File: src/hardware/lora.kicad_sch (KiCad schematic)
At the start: 19 parts

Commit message: Selected GPIO
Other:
- note added: "tcxoVoltage: 0x02 (1.8V)"
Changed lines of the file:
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@@
+		)
+	)
+	(text "tcxoVoltage: 0x02 (1.8V)"
+		(exclude_from_sim no)
+		(at 74.422 86.36 0)
+		(effects
+			(font
+				(size 1.27 1.27)
+			)
 		)
 	)

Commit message: Selected GPIO
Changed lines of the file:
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@@
 		)
 		(property "Value" "GND"
-			(at 132.08 128.27 0)
-			(effects
-				(font
-					(size 1.27 1.27)
-				)
+			(at 134.62 124.4599 0)
+			(effects
+				(font
+					(size 1.27 1.27)
+				)
+				(justify left)
 			)
 		)
@@
 		)
 		(property "Value" "GND"
-			(at 107.95 97.79 0)
-			(effects
-				(font
-					(size 1.27 1.27)
-				)
+			(at 110.49 93.9799 0)
+			(effects
+				(font
+					(size 1.27 1.27)
+				)
+				(justify left)
 			)
 		)
@@
 		)
 		(property "Value" "GND"
-			(at 80.01 102.87 0)
-			(effects
-				(font
-					(size 1.27 1.27)
-				)
-			)
-		)
+			(at 82.55 99.0599 0)
+			(effects
+				(font
+					(size 1.27 1.27)
+				)
+				(justify left)
+			)
+		)

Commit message: LoRa Crystal Optional
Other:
- note added: "Optional"
- moved on the sheet: C?, Q?, R?, Y?

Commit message: Added Accelerometer Clock; Cleanup & Fixes
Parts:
- R?: value 100 -> 100Ω
- R?: value 220 -> 220Ω
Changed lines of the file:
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@@
 			)
 		)
-		(property "Value" "100"
+		(property "Value" "100Ω"
 			(at 67.31 128.2699 0)
 			(effects
@@
 		(fields_autoplaced yes)
 		(property "Reference" "R?"
-			(at 115.57 72.39 90)
-			(effects
-				(font
-					(size 1.27 1.27)
-				)
-			)
-		)
-		(property "Value" "220"
-			(at 115.57 74.93 90)
-			(effects
-				(font
+			(at 115.57 62.23 90)
+			(effects
+				(font
+					(size 1.27 1.27)
+				)
+			)
+		)
+		(property "Value" "220Ω"
+			(at 115.57 64.77 90)
+			(effects
+				(font

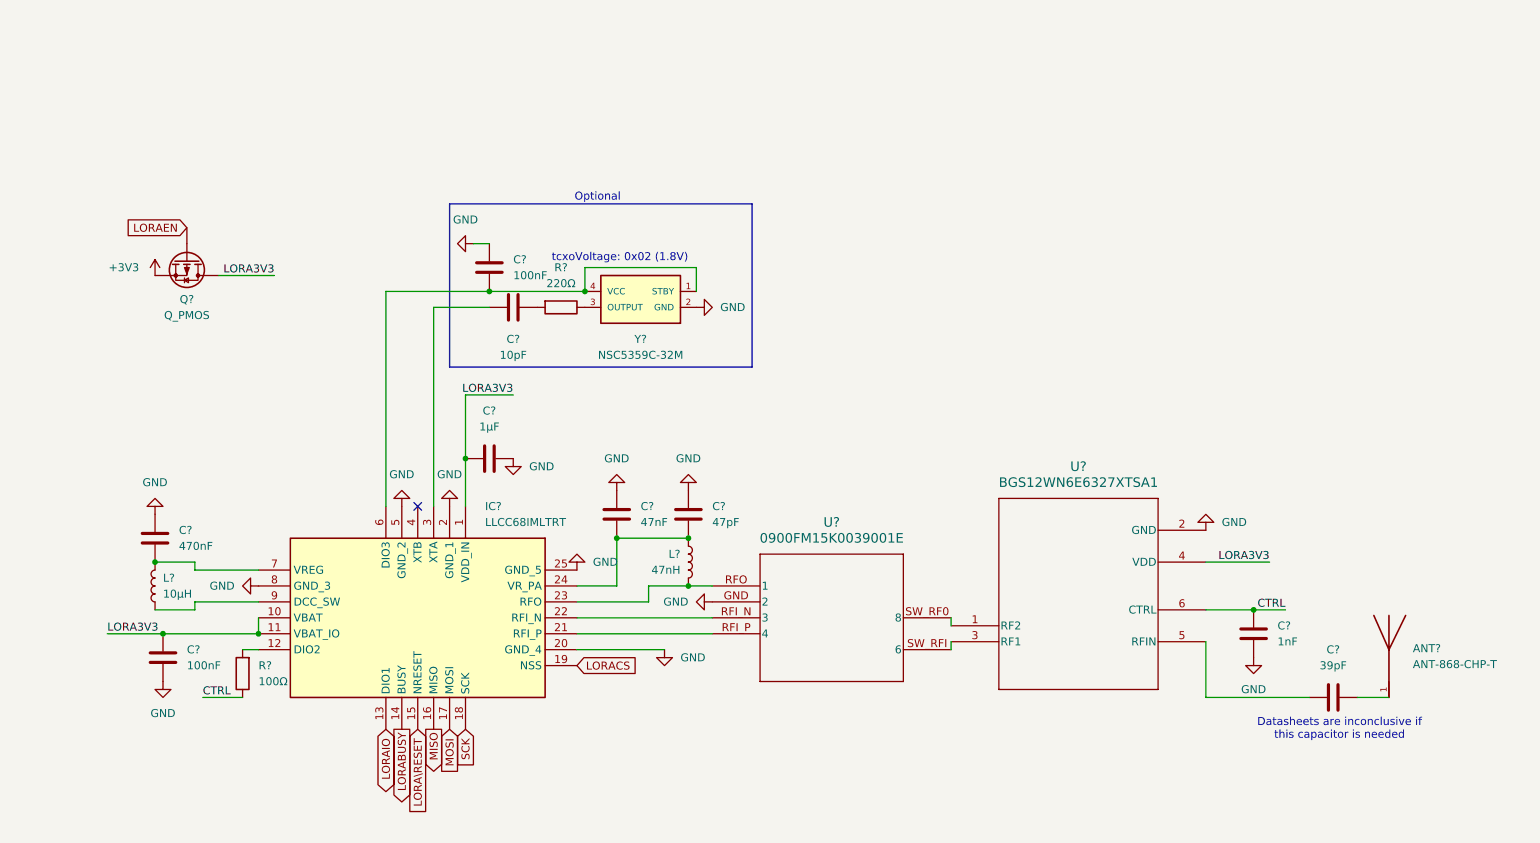
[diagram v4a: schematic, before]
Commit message: Cleanup & Fixes; Added footprints; Removed Light sensors
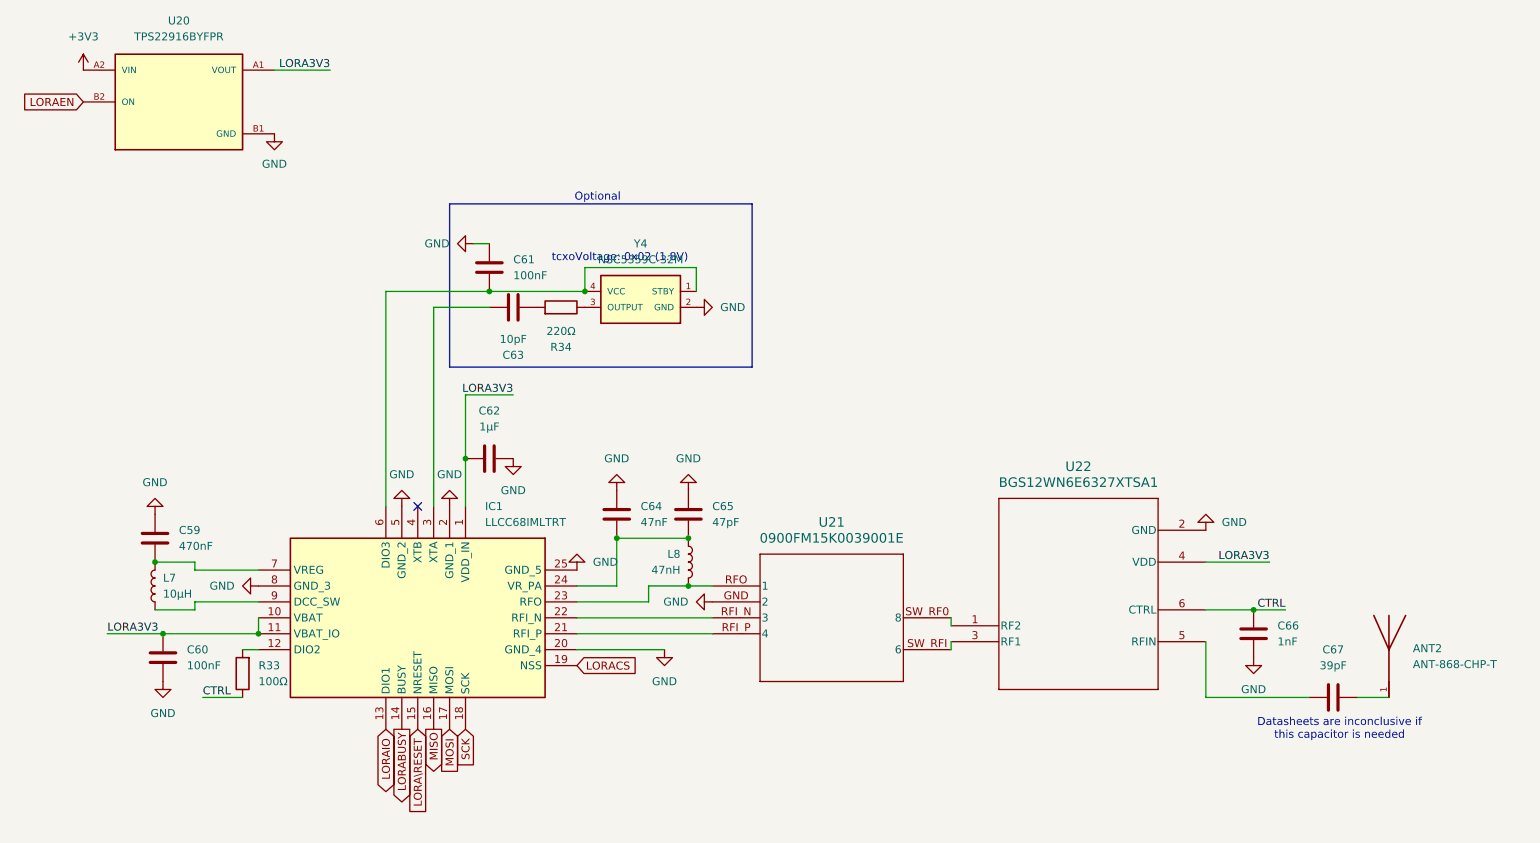
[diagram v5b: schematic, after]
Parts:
- removed Q?: Q_PMOS, symbol Device:Q_PMOS
- added U20: TPS22916BYFPR, Project:IC_TPS22916BYFPR, symbol TPS22916BYFPR:TPS22916BYFPR
- ANT2: renamed from ANT?; footprint ANT-868-CHP-T:XDCR_ANT-868-CHP-T -> Project:XTAL_ABS07-32.768KHZ-7-T
- C59, C60, C61, C62, C63, C64, C65, C66, C67: renamed from C?; footprint (none) -> Capacitor_SMD:C_0603_1608Metric
- IC1: renamed from IC?; footprint QFN50P400X400X100-25L-D -> Project:QFN50P400X400X100-25L-D
- L7, L8: renamed from L?; footprint (none) -> Inductor_SMD:L_0402_1005Metric
- R33, R34: renamed from R?; footprint (none) -> Resistor_SMD:R_0603_1608Metric
- U21: renamed from U?; footprint QFP20P0X0X31-0_JOT -> Project:QFP20P0X0X31-0_JOT
- U22: renamed from U?; footprint PG-TSNP-6-10_INF -> Project:PG-TSNP-6-10_INF
- Y4: renamed from Y?; footprint NSC5359C:NSC5359C -> Project:NSC5359C
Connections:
- net +3V3: now also U20.A2 (VIN)
- net GND: now also U20.B1 (GND)
- net LORA3V3: now also U20.A1 (VOUT)
- net LORAEN: now also U20.B2 (ON)

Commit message: Cleanup & Fixes; Changed GPIO; Added Camera; Added Microphone
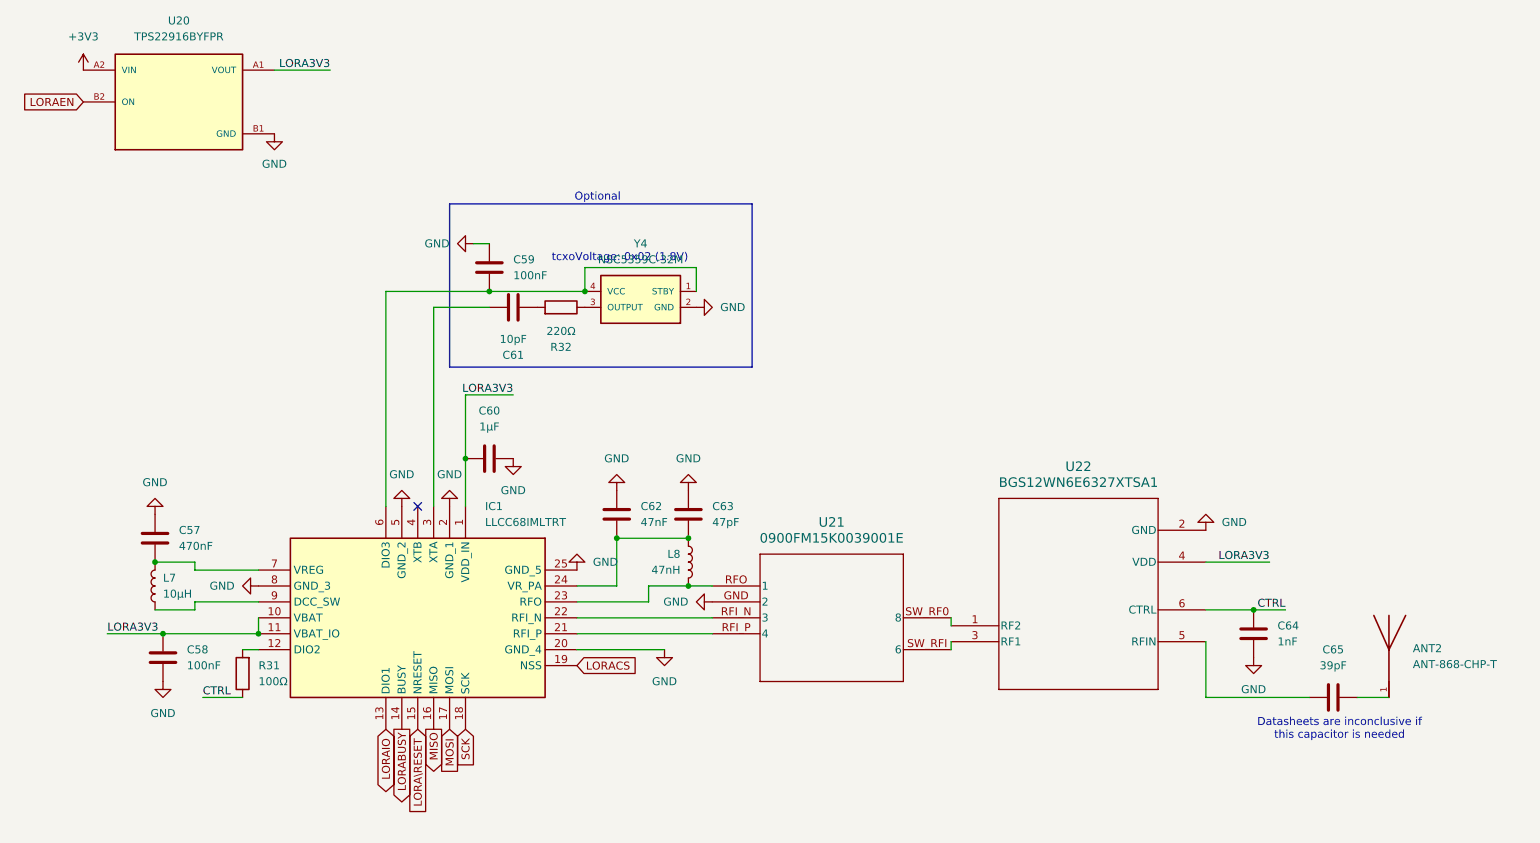
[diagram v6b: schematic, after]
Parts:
- renumbered C59 to C57, C60 to C58, C61 to C59, C62 to C60, C63 to C61, C64 to C62, C65 to C63, C66 to C64, C67 to C65, R33 to R31, R34 to R32
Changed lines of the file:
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@@
 		(dnp no)
 		(fields_autoplaced yes)
-		(property "Reference" "C65"
+		(property "Reference" "C63"
 			(at 139.7 100.3299 0)
 			(effects
@@
 			(project "raywatch"
 				(path "/7b654ee8-2a53-4d39-8b7d-32c7bb3cb0ed/500b48f3-f083-4626-a865-624bdd615c7c"
-					(reference "C65")
+					(reference "C63")
 					(unit 1)
 				)
@@
 		(dnp no)
 		(fields_autoplaced yes)
-		(property "Reference" "C63"
+		(property "Reference" "C61"
 			(at 107.95 76.2 90)
 			(effects
@@
 			(project "raywatch"
 				(path "/7b654ee8-2a53-4d39-8b7d-32c7bb3cb0ed/500b48f3-f083-4626-a865-624bdd615c7c"
-					(reference "C63")
+					(reference "C61")
 					(unit 1)
 				)
@@
 		(dnp no)
 		(fields_autoplaced yes)
-		(property "Reference" "R33"
+		(property "Reference" "R31"
 			(at 67.31 125.7299 0)
 			(effects
@@
 			(project "raywatch"
 				(path "/7b654ee8-2a53-4d39-8b7d-32c7bb3cb0ed/500b48f3-f083-4626-a865-624bdd615c7c"
-					(reference "R33")
+					(reference "R31")
 					(unit 1)
 				)
@@
 		(dnp no)
 		(fields_autoplaced yes)
-		(property "Reference" "#PWR0334"
+		(property "Reference" "#PWR0330"
 			(at 132.08 129.54 0)
 			(effects
@@
 			(project "raywatch"
 				(path "/7b654ee8-2a53-4d39-8b7d-32c7bb3cb0ed/500b48f3-f083-4626-a865-624bdd615c7c"
-					(reference "#PWR0334")
+					(reference "#PWR0330")
 					(unit 1)
 				)
@@
 		(dnp no)
 		(fields_autoplaced yes)
-		(property "Reference" "C60"
+		(property "Reference" "C58"
 			(at 55.88 123.1899 0)
 			(effects
@@
 			(project "raywatch"
 				(path "/7b654ee8-2a53-4d39-8b7d-32c7bb3cb0ed/500b48f3-f083-4626-a865-624bdd615c7c"
-					(reference "C60")
+					(reference "C58")
 					(unit 1)
 				)
@@
 		(dnp no)
 		(fields_autoplaced yes)
-		(property "Reference" "#PWR0324"
+		(property "Reference" "#PWR0320"
 			(at 50.8 95.25 0)
 			(effects
@@
 			(project "raywatch"
 				(path "/7b654ee8-2a53-4d39-8b7d-32c7bb3cb0ed/500b48f3-f083-4626-a865-624bdd615c7c"
-					(reference "#PWR0324")
+					(reference "#PWR0320")
 					(unit 1)
 				)
@@
 		(dnp no)
 		(fields_autoplaced yes)
-		(property "Reference" "#PWR0325"
+		(property "Reference" "#PWR0321"
 			(at 52.07 134.62 0)
 			(effects
@@
 			(project "raywatch"
 				(path "/7b654ee8-2a53-4d39-8b7d-32c7bb3cb0ed/500b48f3-f083-4626-a865-624bdd615c7c"
-					(reference "#PWR0325")
+					(reference "#PWR0321")
 					(unit 1)
 				)
@@
 		(dnp no)
 		(fields_autoplaced yes)
-		(property "Reference" "#PWR0326"
+		(property "Reference" "#PWR0322"
 			(at 60.96 113.03 0)
 			(effects
@@
 			(project "raywatch"
 				(path "/7b654ee8-2a53-4d39-8b7d-32c7bb3cb0ed/500b48f3-f083-4626-a865-624bdd615c7c"
-					(reference "#PWR0326")
+					(reference "#PWR0322")
 					(unit 1)
 				)
@@
 		(dnp no)
 		(fields_autoplaced yes)
-		(property "Reference" "#PWR0327"
+		(property "Reference" "#PWR0323"
 			(at 69.85 47.244 0)
 			(effects
@@
 			(project "raywatch"
 				(path "/7b654ee8-2a53-4d39-8b7d-32c7bb3cb0ed/500b48f3-f083-4626-a865-624bdd615c7c"
-					(reference "#PWR0327")
+					(reference "#PWR0323")
 					(unit 1)
 				)
@@
 		(dnp no)
 		(fields_autoplaced yes)
-		(property "Reference" "C62"
+		(property "Reference" "C60"
 			(at 104.14 85.09 90)
 			(effects
@@
 			(project "raywatch"
 				(path "/7b654ee8-2a53-4d39-8b7d-32c7bb3cb0ed/500b48f3-f083-4626-a865-624bdd615c7c"
-					(reference "C62")
+					(reference "C60")
 					(unit 1)
 				)
@@
 		(dnp no)
 		(fields_autoplaced yes)
-		(property "Reference" "#PWR0337"
+		(property "Reference" "#PWR0333"
 			(at 133.35 115.57 0)
 			(effects
@@
 			(project "raywatch"
 				(path "/7b654ee8-2a53-4d39-8b7d-32c7bb3cb0ed/500b48f3-f083-4626-a865-624bdd615c7c"
-					(reference "#PWR0337")
+					(reference "#PWR0333")
 					(unit 1)
 				)
@@
 		(dnp no)
 		(fields_autoplaced yes)
-		(property "Reference" "R34"
+		(property "Reference" "R32"
 			(at 115.57 74.93 90)
 			(effects
@@
 			(project "raywatch"
 				(path "/7b654ee8-2a53-4d39-8b7d-32c7bb3cb0ed/500b48f3-f083-4626-a865-624bdd615c7c"
-					(reference "R34")
+					(reference "R32")
 					(unit 1)
 				)
@@
 		(dnp no)
 		(fields_autoplaced yes)
-		(property "Reference" "#PWR0331"
+		(property "Reference" "#PWR0327"
 			(at 107.95 99.06 0)
 			(effects
@@
 			(project "raywatch"
 				(path "/7b654ee8-2a53-4d39-8b7d-32c7bb3cb0ed/500b48f3-f083-4626-a865-624bdd615c7c"
-					(reference "#PWR0331")
+					(reference "#PWR0327")
 					(unit 1)
 				)
@@
 		(dnp no)
 		(fields_autoplaced yes)
-		(property "Reference" "#PWR0338"
+		(property "Reference" "#PWR0334"
 			(at 218.44 97.79 0)
 			(effects
@@
 			(project "raywatch"
 				(path "/7b654ee8-2a53-4d39-8b7d-32c7bb3cb0ed/500b48f3-f083-4626-a865-624bdd615c7c"
-					(reference "#PWR0338")
+					(reference "#PWR0334")
 					(unit 1)
 				)
@@
 		(dnp no)
 		(fields_autoplaced yes)
-		(property "Reference" "C66"
+		(property "Reference" "C64"
 			(at 229.87 119.3799 0)
 			(effects
@@
 			(project "raywatch"
 				(path "/7b654ee8-2a53-4d39-8b7d-32c7bb3cb0ed/500b48f3-f083-4626-a865-624bdd615c7c"
-					(reference "C66")
+					(reference "C64")
 					(unit 1)
 				)
@@
 		(dnp no)
 		(fields_autoplaced yes)
-		(property "Reference" "#PWR0333"
+		(property "Reference" "#PWR0329"
 			(at 124.46 91.44 0)
 			(effects
@@
 			(project "raywatch"
 				(path "/7b654ee8-2a53-4d39-8b7d-32c7bb3cb0ed/500b48f3-f083-4626-a865-624bdd615c7c"
-					(reference "#PWR0333")
+					(reference "#PWR0329")
 					(unit 1)
 				)
@@
 		(dnp no)
 		(fields_autoplaced yes)
-		(property "Reference" "#PWR0335"
+		(property "Reference" "#PWR0331"
 			(at 135.89 91.44 0)
 			(effects
@@
 			(project "raywatch"
 				(path "/7b654ee8-2a53-4d39-8b7d-32c7bb3cb0ed/500b48f3-f083-4626-a865-624bdd615c7c"
-					(reference "#PWR0335")
+					(reference "#PWR0331")
 					(unit 1)
 				)
@@
 		(dnp no)
 		(fields_autoplaced yes)
-		(property "Reference" "C61"
+		(property "Reference" "C59"
 			(at 107.95 60.9599 0)
 			(effects
@@
 			(project "raywatch"
 				(path "/7b654ee8-2a53-4d39-8b7d-32c7bb3cb0ed/500b48f3-f083-4626-a865-624bdd615c7c"
-					(reference "C61")
+					(reference "C59")
 					(unit 1)
 				)
@@
 		(dnp no)
 		(fields_autoplaced yes)
-		(property "Reference" "#PWR0329"
+		(property "Reference" "#PWR0325"
 			(at 97.79 93.98 0)
 			(effects
@@
 			(project "raywatch"
 				(path "/7b654ee8-2a53-4d39-8b7d-32c7bb3cb0ed/500b48f3-f083-4626-a865-624bdd615c7c"
-					(reference "#PWR0329")
+					(reference "#PWR0325")
 					(unit 1)
 				)
@@
 		(dnp no)
 		(fields_autoplaced yes)
-		(property "Reference" "C64"
+		(property "Reference" "C62"
 			(at 128.27 100.3299 0)
 			(effects
@@
 			(project "raywatch"
 				(path "/7b654ee8-2a53-4d39-8b7d-32c7bb3cb0ed/500b48f3-f083-4626-a865-624bdd615c7c"
-					(reference "C64")
+					(reference "C62")
 					(unit 1)
 				)
@@
 		(dnp no)
 		(fields_autoplaced yes)
-		(property "Reference" "C67"
+		(property "Reference" "C65"
 			(at 238.76 123.19 90)
 			(effects
@@
 			(project "raywatch"
 				(path "/7b654ee8-2a53-4d39-8b7d-32c7bb3cb0ed/500b48f3-f083-4626-a865-624bdd615c7c"
-					(reference "C67")
+					(reference "C65")
 					(unit 1)
 				)
@@
 		(dnp no)
 		(fields_autoplaced yes)
-		(property "Reference" "#PWR0323"
+		(property "Reference" "#PWR0319"
 			(at 39.37 34.544 0)
 			(effects
@@
 			(project "raywatch"
 				(path "/7b654ee8-2a53-4d39-8b7d-32c7bb3cb0ed/500b48f3-f083-4626-a865-624bdd615c7c"
-					(reference "#PWR0323")
+					(reference "#PWR0319")
 					(unit 1)
 				)
@@
 		(dnp no)
 		(fields_autoplaced yes)
-		(property "Reference" "#PWR0330"
+		(property "Reference" "#PWR0326"
 			(at 95.25 58.42 0)
 			(effects
@@
 			(project "raywatch"
 				(path "/7b654ee8-2a53-4d39-8b7d-32c7bb3cb0ed/500b48f3-f083-4626-a865-624bdd615c7c"
-					(reference "#PWR0330")
+					(reference "#PWR0326")
 					(unit 1)
 				)
@@
 		(dnp no)
 		(fields_autoplaced yes)
-		(property "Reference" "C59"
+		(property "Reference" "C57"
 			(at 54.61 104.1399 0)
 			(effects
@@
 			(project "raywatch"
 				(path "/7b654ee8-2a53-4d39-8b7d-32c7bb3cb0ed/500b48f3-f083-4626-a865-624bdd615c7c"
-					(reference "C59")
+					(reference "C57")
 					(unit 1)
 				)
@@
 		(dnp no)
 		(fields_autoplaced yes)
-		(property "Reference" "#PWR0336"
+		(property "Reference" "#PWR0332"
 			(at 143.51 68.58 0)
 			(effects
@@
 			(project "raywatch"
 				(path "/7b654ee8-2a53-4d39-8b7d-32c7bb3cb0ed/500b48f3-f083-4626-a865-624bdd615c7c"
-					(reference "#PWR0336")
+					(reference "#PWR0332")
 					(unit 1)
 				)
@@
 		(dnp no)
 		(fields_autoplaced yes)
-		(property "Reference" "#PWR0328"
+		(property "Reference" "#PWR0324"
 			(at 90.17 93.98 0)
 			(effects
@@
 			(project "raywatch"
 				(path "/7b654ee8-2a53-4d39-8b7d-32c7bb3cb0ed/500b48f3-f083-4626-a865-624bdd615c7c"
-					(reference "#PWR0328")
+					(reference "#PWR0324")
 					(unit 1)
 				)
@@
 		(dnp no)
 		(fields_autoplaced yes)
-		(property "Reference" "#PWR0339"
+		(property "Reference" "#PWR0335"
 			(at 226.06 130.81 0)
 			(effects
@@
 			(project "raywatch"
 				(path "/7b654ee8-2a53-4d39-8b7d-32c7bb3cb0ed/500b48f3-f083-4626-a865-624bdd615c7c"
-					(reference "#PWR0339")
+					(reference "#PWR0335")
 					(unit 1)
 				)
@@
 		(dnp no)
 		(fields_autoplaced yes)
-		(property "Reference" "#PWR0332"
+		(property "Reference" "#PWR0328"
 			(at 118.11 104.14 0)
 			(effects
@@
 			(project "raywatch"
 				(path "/7b654ee8-2a53-4d39-8b7d-32c7bb3cb0ed/500b48f3-f083-4626-a865-624bdd615c7c"
-					(reference "#PWR0332")
-					(unit 1)
-				)
+					(reference "#PWR0328")
+					(unit 1)
+				)
